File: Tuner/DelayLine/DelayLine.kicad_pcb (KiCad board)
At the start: 2 copper layers, 100 x 100 mm, 86 parts, among them J1 Conn_Coaxial, J10 Conn_Coaxial, J11 Conn_Coaxial, J12 Conn_Coaxial, J13 Conn_01x01, J14 Conn_01x01, J15 Conn_01x01, J16 Conn_01x01, J17 Conn_02x10_Odd_Even, J18 Conn_Coaxial, J19 Conn_Coaxial, J2 Conn_01x01, J20 Conn_Coaxial, J21 Conn_Coaxial, J22 Conn_Coaxial, J23 Conn_Coaxial, J24 Conn_01x01, J25 Conn_01x01, J26 Conn_01x01, J27 Conn_01x01, J28 Conn_01x01, J29 Conn_Coaxial, J3 Conn_Coaxial, J31 Conn_Coaxial, J32 Conn_01x01, J33 Conn_01x01, J34 Conn_01x01, J35 Conn_01x01, J5 Conn_Coaxial, J6 Conn_Coaxial, J7 Conn_Coaxial, J8 Conn_01x02, J9 Conn_01x02

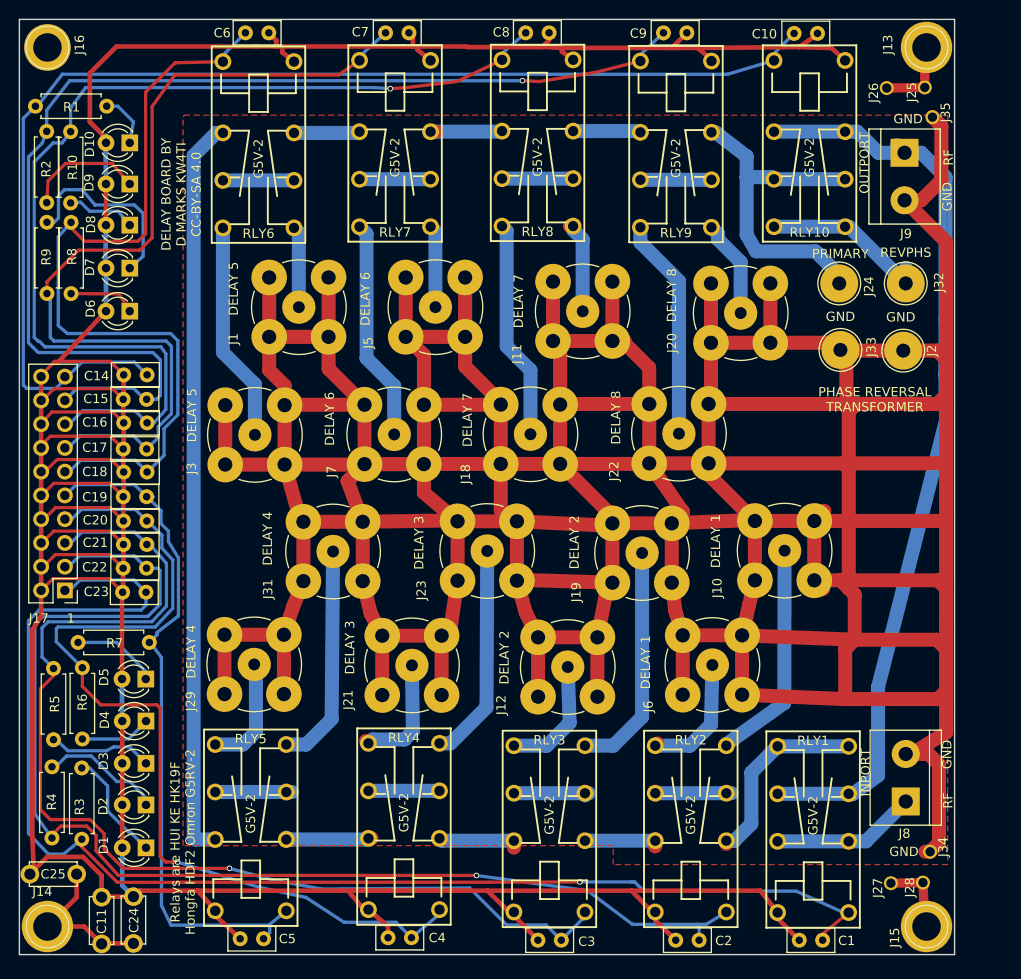
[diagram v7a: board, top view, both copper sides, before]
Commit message: Added BNC and screw terminal combo pads
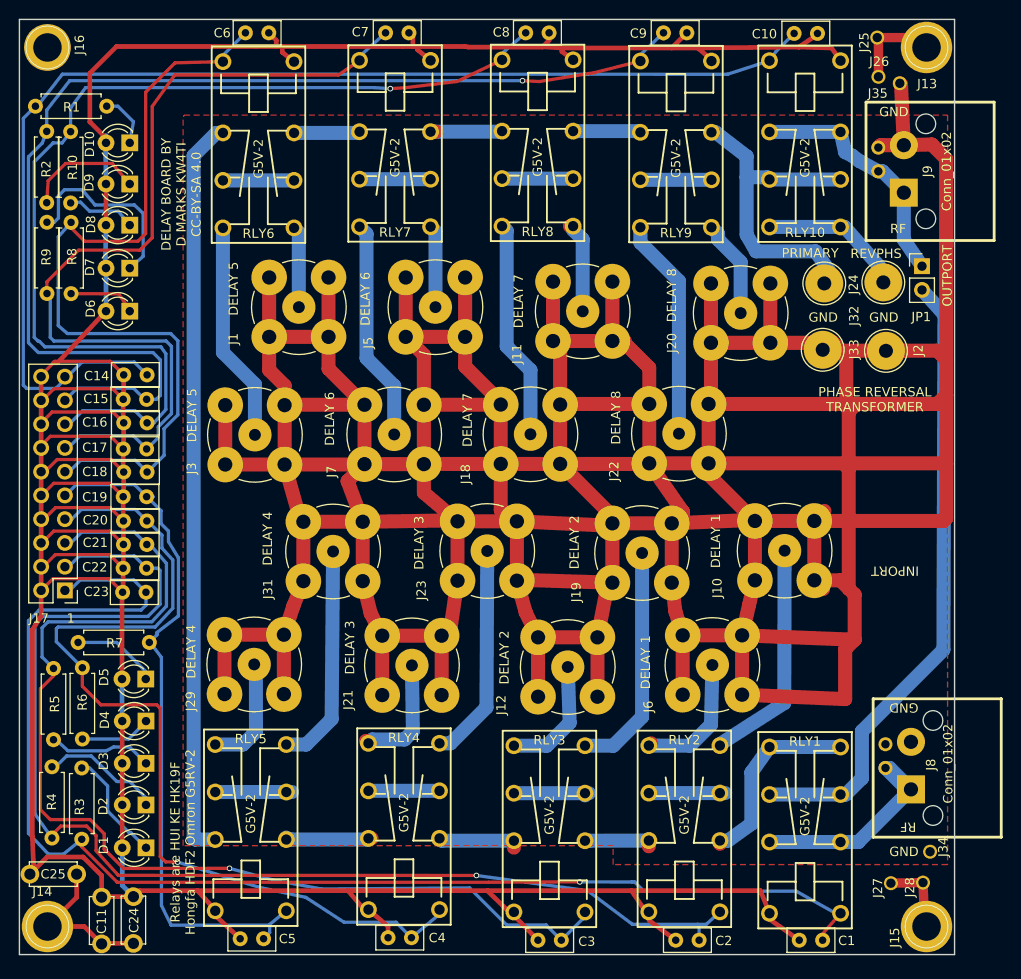
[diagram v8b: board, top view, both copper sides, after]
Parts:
- added JP1: Jumper_NC_Small, Pin_Headers:Pin_Header_Straight_1x02_Pitch2.54mm, F.Cu at (146.5, 76.4)
- J8, J9: footprint Connectors_Terminal_Blocks:TerminalBlock_bornier-2_P5.08mm -> tuner:bnc_90_1-1337543-0_pad_combo
- moved J8 10.8 mm to (155.0, 130.0)
- moved J9 9.78 mm to (154.2, 66.2), turned to 90 degrees
- moved J25 7.37 mm to (140.5, 51.9)
- moved J35 5.03 mm to (145.4, 56.8)
- moved J32 2.40 mm to (142.4, 78.1)
- moved J33 1.89 mm to (135.9, 85.3)
- moved J2 1.85 mm to (142.7, 85.4)
- moved J24 1.60 mm to (136.1, 78.2)
- moved J26 1.50 mm to (140.6, 56.1)
- moved RLY1 0.87 mm to (134.0, 143.2)
- moved RLY2 0.69 mm to (121.1, 143.1)
- moved RLY10 0.48 mm to (134.0, 56.8)
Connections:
- RLY1 pad 3: RFOUT -> Net-(JP1-Pad2)
- RLY1 pad 7: RFOUT -> Net-(JP1-Pad2)
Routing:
- net RFOUT: track 97.8 -> 26.1 mm
- net RFGND: track 854.2 -> 783.3 mm
- net Net-(JP1-Pad2): track 0.00 -> 67.8 mm
- net RFSIG: track 15.5 -> 24.8 mm
- net Net-(J32-Pad1): track 18.2 -> 16.0 mm
- net Net-(J13-Pad1): track 10.8 -> 12.6 mm
- net RLY1: track 144.4 -> 143.0 mm
- net Net-(J24-Pad1): track 37.3 -> 36.3 mm
- net Net-(J6-Pad1): track 13.8 -> 14.5 mm
- net Net-(RLY2-Pad2): track 8.78 -> 8.10 mm
- net Net-(J10-Pad1): track 24.0 -> 24.6 mm
- net RLY2: track 133.2 -> 132.7 mm
